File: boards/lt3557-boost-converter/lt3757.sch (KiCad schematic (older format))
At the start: 21 parts

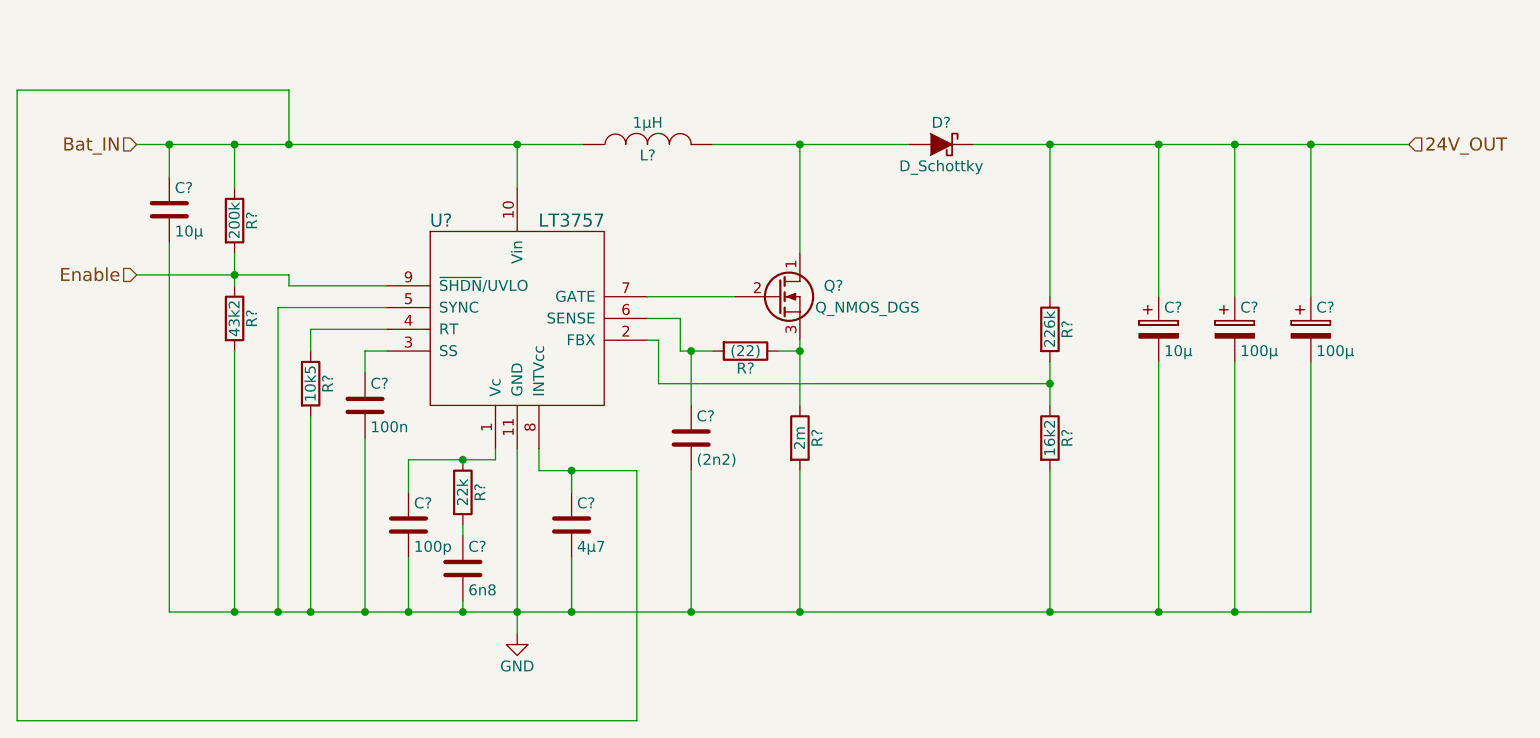
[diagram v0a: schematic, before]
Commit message: lt3557-boost-converter: schematic finished; parts selected; footprints assigned
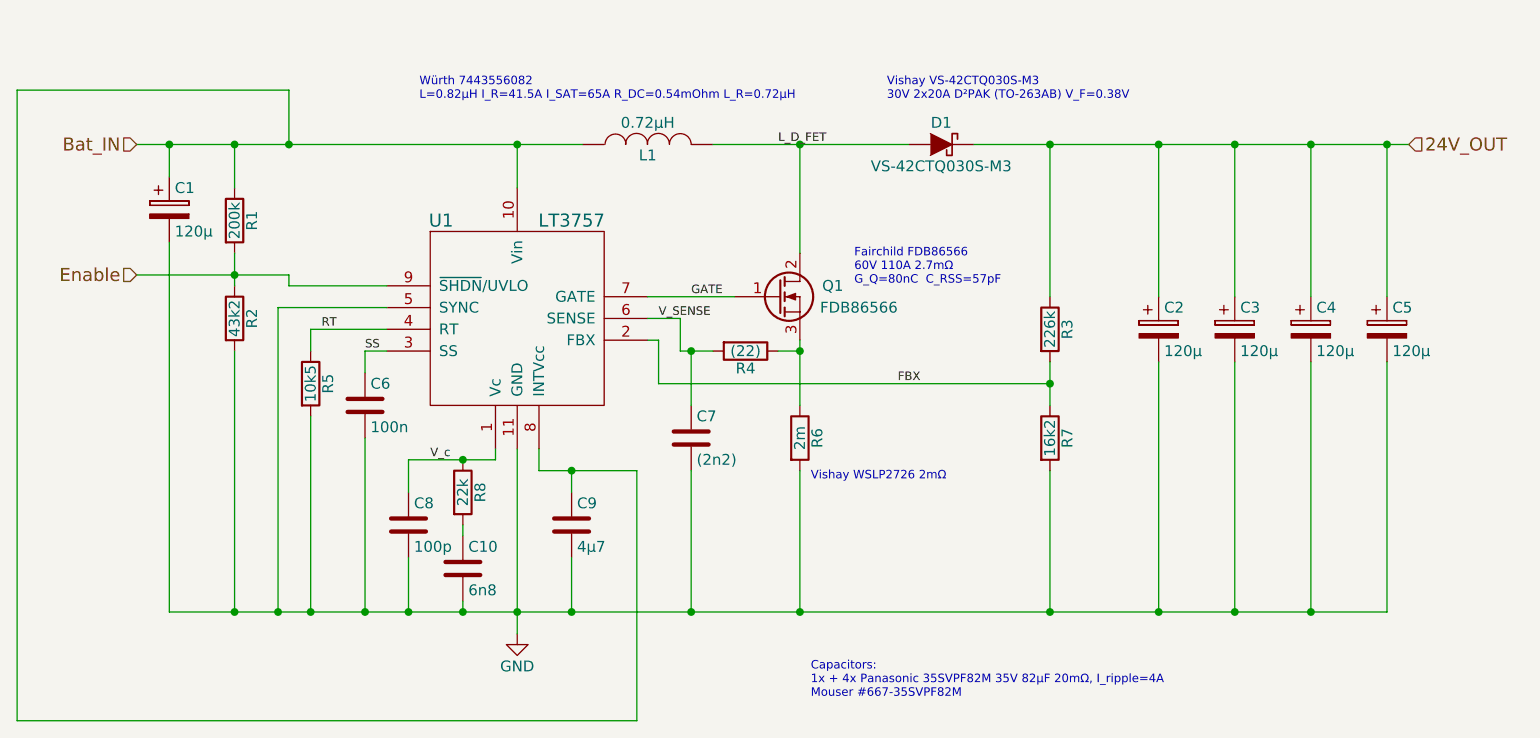
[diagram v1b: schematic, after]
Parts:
- removed C?: 10µ, symbol C
- removed Q?: Q_NMOS_DGS, symbol Q_NMOS_DGS
- added C1: 120µ, Capacitors_SMD:c_elec_8x10.5, symbol CP
- added C5: 120µ, Capacitors_SMD:c_elec_10x10.5, symbol CP
- added Q1: FDB86566, Diodes_SMD:DD-PAK_TO263_DualDiode_ThermalVias, symbol Q_NMOS_GDS
- C10, C6, C7, C8: renamed from C?; footprint (none) -> Capacitors_SMD:C_0603
- C2: renamed from C?; value 10µ -> 120µ; footprint (none) -> Capacitors_SMD:c_elec_8x10.5
- C3, C4: renamed from C?; value 100µ -> 120µ; footprint (none) -> Capacitors_SMD:c_elec_8x10.5
- C9: renamed from C?; footprint (none) -> Capacitors_SMD:C_0805
- D1: renamed from D?; value D_Schottky -> VS-42CTQ030S-M3; footprint (none) -> Diodes_SMD:DD-PAK_TO263_DualDiode_ThermalVias
- L1: renamed from L?; value 1µH -> 0.72µH; footprint (none) -> GH_Inductors:Inductor_Wurth_HCI-1890
- R1, R2, R3, R4, R5, R7, R8: renamed from R?; footprint (none) -> Resistors_SMD:R_0603
- R6: renamed from R?; footprint (none) -> resistor-power-shunt:WSLP2726
- U1: renamed from U?; footprint (none) -> Housings_SSOP:MSOP-10-1EP_3x3mm_Pitch0.5mm
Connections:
- net 24V_OUT: now also C5.1
- net Bat_IN: now also C1.1
- net GND: now also C1.2, C5.2
- net V_c: now reaches C8.1, R8.1, U1.1 (Vc)
- net FBX: now reaches R3.2, R7.1, U1.2 (FBX)
- net SS: now reaches C6.1, U1.3 (SS)
- net RT: now reaches R5.1, U1.4 (RT)
- net V_SENSE: now reaches C7.1, R4.2, U1.6 (SENSE)
- net GATE: now reaches U1.7 (GATE)
- net GATE: now also Q1.1 (G)
- net L_D_FET: now reaches D1.2 (A), L1.2
- net L_D_FET: now also Q1.2 (D)
- net at R4.1, R6.1: now also Q1.3 (S)
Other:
- note added: "Capacitors:\n1x + 4x Panasonic 35SVPF82M 35V 82µF 20mΩ, I_ripple=4A\nMouser #667-35SVPF82M"
- note added: "Fairchild FDB86566\n60V 110A 2.7mΩ\nG_Q=80nC C_RSS=57pF"
- note added: "Vishay VS-42CTQ030S-M3\n30V 2x20A D²PAK (TO-263AB) V_F=0.38V"
- note added: "Vishay WSLP2726 2mΩ"
- note added: "Würth 7443556082\nL=0.82µH I_R=41.5A I_SAT=65A R_DC=0.54mOhm L_R=0.72µH"
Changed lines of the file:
@@
 24V_OUT
 $Comp
-L GND #PWR?
+L GND #PWR03
 U 1 1 588F90A8
 P 4600 3550
-F 0 "#PWR?" H 4600 3300 50  0001 C CNN
+F 0 "#PWR03" H 4600 3300 50  0001 C CNN
 F 1 "GND" H 4600 3400 50  0000 C CNN
 F 2 "" H 4600 3550 50  0000 C CNN
@@
 Enable
 $Comp
-L LT3757 U?
+L LT3757 U1
 U 1 1 588F9C46
 P 4600 2100
-F 0 "U?" H 4250 2550 60  0000 C CNN
+F 0 "U1" H 4250 2550 60  0000 C CNN
 F 1 "LT3757" H 4850 2550 60  0000 C CNN
-F 2 "" H 4600 2100 60  0001 C CNN
+F 2 "Housings_SSOP:MSOP-10-1EP_3x3mm_Pitch0.5mm" H 4600 2100 60  0001 C CNN
 F 3 "" H 4600 2100 60  0001 C CNN
 	1    4600 2100
@@
 	4600 1300 4600 1500
 $Comp
-L INDUCTOR L?
+L INDUCTOR L1
 U 1 1 588F9D48
 P 5200 1300
-F 0 "L?" V 5150 1300 50  0000 C CNN
-F 1 "1µH" V 5300 1300 50  0000 C CNN
-F 2 "" H 5200 1300 50  0000 C CNN
+F 0 "L1" V 5150 1300 50  0000 C CNN
+F 1 "0.72µH" V 5300 1300 50  0000 C CNN
+F 2 "GH_Inductors:Inductor_Wurth_HCI-1890" H 5200 1300 50  0001 C CNN
 F 3 "" H 5200 1300 50  0000 C CNN
 	1    5200 1300
@@
 $EndComp
 $Comp
-L D_Schottky D?
+L D_Schottky D1
 U 1 1 588F9DE1
 P 6550 1300
-F 0 "D?" H 6550 1400 50  0000 C CNN
-F 1 "D_Schottky" H 6550 1200 50  0000 C CNN
-F 2 "" H 6550 1300 50  0000 C CNN
+F 0 "D1" H 6550 1400 50  0000 C CNN
+F 1 "VS-42CTQ030S-M3" H 6550 1200 50  0000 C CNN
+F 2 "Diodes_SMD:DD-PAK_TO263_DualDiode_ThermalVias" H 6550 1300 50  0001 C CNN
 F 3 "" H 6550 1300 50  0000 C CNN
 	1    6550 1300
@@
 $EndComp
 $Comp
-L Q_NMOS_DGS Q?
-U 1 1 588F9EA6
-P 5800 2000
-F 0 "Q?" H 6100 2050 50  0000 R CNN
-F 1 "Q_NMOS_DGS" H 6450 1950 50  0000 R CNN
-F 2 "" H 6000 2100 50  0000 C CNN
-F 3 "" H 5800 2000 50  0000 C CNN
-	1    5800 2000
-	1    0    0    -1
-$EndComp
-$Comp
-L R R?
+L R R6
 U 1 1 588F9F5B
 P 5900 2650
-F 0 "R?" V 5980 2650 50  0000 C CNN
+F 0 "R6" V 5980 2650 50  0000 C CNN
 F 1 "2m" V 5900 2650 50  0000 C CNN
-F 2 "" V 5830 2650 50  0000 C CNN
+F 2 "resistor-power-shunt:WSLP2726" V 5830 2650 50  0001 C CNN
 F 3 "" H 5900 2650 50  0000 C CNN
 	1    5900 2650
@@
 $EndComp
 $Comp
-L R R?
+L R R3
 U 1 1 588FA0E6
 P 7050 2150
-F 0 "R?" V 7130 2150 50  0000 C CNN
+F 0 "R3" V 7130 2150 50  0000 C CNN
 F 1 "226k" V 7050 2150 50  0000 C CNN
-F 2 "" V 6980 2150 50  0000 C CNN
+F 2 "Resistors_SMD:R_0603" V 6980 2150 50  0001 C CNN
 F 3 "" H 7050 2150 50  0000 C CNN
 	1    7050 2150
@@
 $EndComp
 $Comp
-L R R?
+L R R7
 U 1 1 588FA11B
 P 7050 2650
-F 0 "R?" V 7130 2650 50  0000 C CNN
+F 0 "R7" V 7130 2650 50  0000 C CNN
 F 1 "16k2" V 7050 2650 50  0000 C CNN
-F 2 "" V 6980 2650 50  0000 C CNN
+F 2 "Resistors_SMD:R_0603" V 6980 2650 50  0001 C CNN
 F 3 "" H 7050 2650 50  0000 C CNN
 	1    7050 2650
@@
 $EndComp
 $Comp
-L CP C?
+L CP C2
 U 1 1 588FA17F
 P 7550 2150
-F 0 "C?" H 7575 2250 50  0000 L CNN
-F 1 "10µ" H 7575 2050 50  0000 L CNN
-F 2 "" H 7588 2000 50  0000 C CNN
+F 0 "C2" H 7575 2250 50  0000 L CNN
+F 1 "120µ" H 7575 2050 50  0000 L CNN
+F 2 "Capacitors_SMD:c_elec_8x10.5" H 7588 2000 50  0001 C CNN
 F 3 "" H 7550 2150 50  0000 C CNN
 	1    7550 2150
@@
 $EndComp
 $Comp
-L CP C?
+L CP C3
 U 1 1 588FA2C0
 P 7900 2150
-F 0 "C?" H 7925 2250 50  0000 L CNN
-F 1 "100µ" H 7925 2050 50  0000 L CNN
-F 2 "" H 7938 2000 50  0000 C CNN
+F 0 "C3" H 7925 2250 50  0000 L CNN
+F 1 "120µ" H 7925 2050 50  0000 L CNN
+F 2 "Capacitors_SMD:c_elec_8x10.5" H 7938 2000 50  0001 C CNN
 F 3 "" H 7900 2150 50  0000 C CNN
 	1    7900 2150
@@
 $EndComp
 $Comp
-L CP C?
+L CP C4
 U 1 1 588FA2F5
 P 8250 2150
-F 0 "C?" H 8275 2250 50  0000 L CNN
-F 1 "100µ" H 8275 2050 50  0000 L CNN
-F 2 "" H 8288 2000 50  0000 C CNN
+F 0 "C4" H 8275 2250 50  0000 L CNN
+F 1 "120µ" H 8275 2050 50  0000 L CNN
+F 2 "Capacitors_SMD:c_elec_8x10.5" H 8288 2000 50  0001 C CNN
 F 3 "" H 8250 2150 50  0000 C CNN
 	1    8250 2150
@@
 $EndComp
 $Comp
-L R R?
+L R R2
 U 1 1 588FA451
 P 3300 2100
-F 0 "R?" V 3380 2100 50  0000 C CNN
+F 0 "R2" V 3380 2100 50  0000 C CNN
 F 1 "43k2" V 3300 2100 50  0000 C CNN
-F 2 "" V 3230 2100 50  0000 C CNN
+F 2 "Resistors_SMD:R_0603" V 3230 2100 50  0001 C CNN
 F 3 "" H 3300 2100 50  0000 C CNN
 	1    3300 2100
@@
 $EndComp
 $Comp
-L R R?
+L R R1
 U 1 1 588FA49A
 P 3300 1650
-F 0 "R?" V 3380 1650 50  0000 C CNN
+F 0 "R1" V 3380 1650 50  0000 C CNN
 F 1 "200k" V 3300 1650 50  0000 C CNN
-F 2 "" V 3230 1650 50  0000 C CNN
+F 2 "Resistors_SMD:R_0603" V 3230 1650 50  0001 C CNN
 F 3 "" H 3300 1650 50  0000 C CNN
 	1    3300 1650
 	1    0    0    -1
 $EndComp
-$Comp
-L C C?
-U 1 1 588FA4D4
-P 3000 1600
-F 0 "C?" H 3025 1700 50  0000 L CNN
-F 1 "10µ" H 3025 1500 50  0000 L CNN
-F 2 "" H 3038 1450 50  0000 C CNN
-F 3 "" H 3000 1600 50  0000 C CNN
-	1    3000 1600
-	1    0    0    -1
-$EndComp
 Wire Wire Line
 	3000 1450 3000 1300
@@
 	3000 1750 3000 3450
 $Comp
-L R R?
+L R R5
 U 1 1 588FA63C
 P 3650 2400
-F 0 "R?" V 3730 2400 50  0000 C CNN
+F 0 "R5" V 3730 2400 50  0000 C CNN
 F 1 "10k5" V 3650 2400 50  0000 C CNN
-F 2 "" V 3580 2400 50  0000 C CNN
+F 2 "Resistors_SMD:R_0603" V 3580 2400 50  0001 C CNN
 F 3 "" H 3650 2400 50  0000 C CNN
 	1    3650 2400
@@
 $EndComp
 $Comp
-L C C?
+L C C6
 U 1 1 588FA6E1
 P 3900 2500
-F 0 "C?" H 3925 2600 50  0000 L CNN
+F 0 "C6" H 3925 2600 50  0000 L CNN
 F 1 "100n" H 3925 2400 50  0000 L CNN
-F 2 "" H 3938 2350 50  0000 C CNN
+F 2 "Capacitors_SMD:C_0603" H 3938 2350 50  0001 C CNN
 F 3 "" H 3900 2500 50  0000 C CNN
 	1    3900 2500
@@
 	3500 2050 3500 3450
 Wire Wire Line
-	3000 3450 8250 3450
+	3000 3450 8600 3450
 Wire Wire Line
 	4600 2700 4600 3550
@@
 Connection ~ 8250 1300
 $Comp
-L R R?
+L R R8
 U 1 1 588FB43F
 P 4350 2900
-F 0 "R?" V 4430 2900 50  0000 C CNN
+F 0 "R8" V 4430 2900 50  0000 C CNN
 F 1 "22k" V 4350 2900 50  0000 C CNN
-F 2 "" V 4280 2900 50  0000 C CNN
+F 2 "Resistors_SMD:R_0603" V 4280 2900 50  0001 C CNN
 F 3 "" H 4350 2900 50  0000 C CNN
 	1    4350 2900
@@
 $EndComp
 $Comp
-L C C?
+L C C10
 U 1 1 588FB4B3
 P 4350 3250
-F 0 "C?" H 4375 3350 50  0000 L CNN
+F 0 "C10" H 4375 3350 50  0000 L CNN
 F 1 "6n8" H 4375 3150 50  0000 L CNN
-F 2 "" H 4388 3100 50  0000 C CNN
+F 2 "Capacitors_SMD:C_0603" H 4388 3100 50  0001 C CNN
 F 3 "" H 4350 3250 50  0000 C CNN
 	1    4350 3250
@@
 	4500 2750 4500 2700
 $Comp
-L C C?
+L C C9
 U 1 1 588FB818
 P 4850 3050
-F 0 "C?" H 4875 3150 50  0000 L CNN
+F 0 "C9" H 4875 3150 50  0000 L CNN
 F 1 "4µ7" H 4875 2950 50  0000 L CNN
-F 2 "" H 4888 2900 50  0000 C CNN
+F 2 "Capacitors_SMD:C_0805" H 4888 2900 50  0001 C CNN
 F 3 "" H 4850 3050 50  0000 C CNN
 	1    4850 3050
@@
 Connection ~ 4850 2800
 $Comp
-L C C?
+L C C8
 U 1 1 588FE63C
 P 4100 3050
-F 0 "C?" H 4125 3150 50  0000 L CNN
+F 0 "C8" H 4125 3150 50  0000 L CNN
 F 1 "100p" H 4125 2950 50  0000 L CNN
-F 2 "" H 4138 2900 50  0000 C CNN
+F 2 "Capacitors_SMD:C_0603" H 4138 2900 50  0001 C CNN
 F 3 "" H 4100 3050 50  0000 C CNN
 	1    4100 3050
@@
 	5250 2200 5250 2400
 $Comp
-L R R?
+L R R4
 U 1 1 588FE946
 P 5650 2250
-F 0 "R?" V 5730 2250 50  0000 C CNN
+F 0 "R4" V 5730 2250 50  0000 C CNN
 F 1 "(22)" V 5650 2250 50  0000 C CNN
-F 2 "" V 5580 2250 50  0000 C CNN
+F 2 "Resistors_SMD:R_0603" V 5580 2250 50  0001 C CNN
 F 3 "" H 5650 2250 50  0000 C CNN
 	1    5650 2250
@@
 $EndComp
 $Comp
-L C C?
+L C C7
 U 1 1 588FE99D
 P 5400 2650
-F 0 "C?" H 5425 2750 50  0000 L CNN
+F 0 "C7" H 5425 2750 50  0000 L CNN
 F 1 "(2n2)" H 5425 2550 50  0000 L CNN
-F 2 "" H 5438 2500 50  0000 C CNN
+F 2 "Capacitors_SMD:C_0603" H 5438 2500 50  0001 C CNN
 F 3 "" H 5400 2650 50  0000 C CNN
 	1    5400 2650
@@
 	5400 2800 5400 3450
 Connection ~ 5400 3450
+Text Notes 4150 1100 0    39   ~ 0
+Würth 7443556082\nL=0.82µH I_R=41.5A I_SAT=65A R_DC=0.54mOhm L_R=0.72µH
+Text Notes 6300 1100 0    39   ~ 0
+Vishay VS-42CTQ030S-M3\n30V 2x20A D²PAK (TO-263AB) V_F=0.38V
+$Comp
+L CP C1
+U 1 1 58924C20
+P 3000 1600
+F 0 "C1" H 3025 1700 50  0000 L CNN
+F 1 "120µ" H 3025 1500 50  0000 L CNN
+F 2 "Capacitors_SMD:c_elec_8x10.5" H 3038 1450 50  0001 C CNN
+F 3 "" H 3000 1600 50  0000 C CNN
+	1    3000 1600
+	1    0    0    -1
+$EndComp
+Text Notes 5950 3850 0    39   ~ 0
+Capacitors:\n1x + 4x Panasonic 35SVPF82M 35V 82µF 20mΩ, I_ripple=4A\nMouser #667-35SVPF82M
+$Comp
+L CP C5
+U 1 1 58924E09
+P 8600 2150
+F 0 "C5" H 8625 2250 50  0000 L CNN
+F 1 "120µ" H 8625 2050 50  0000 L CNN
+F 2 "Capacitors_SMD:c_elec_10x10.5" H 8638 2000 50  0001 C CNN
+F 3 "" H 8600 2150 50  0000 C CNN
+	1    8600 2150
+	1    0    0    -1
+$EndComp
+Wire Wire Line
+	8600 2000 8600 1300
+Connection ~ 8600 1300
+Wire Wire Line
+	8600 3450 8600 2300
+Connection ~ 8250 3450
+Text Notes 5950 2850 0    39   ~ 0
+Vishay WSLP2726 2mΩ
+$Comp
+L Q_NMOS_GDS Q1
+U 1 1 58928FBF
+P 5800 2000
+F 0 "Q1" H 6100 2050 50  0000 R CNN
+F 1 "FDB86566" H 6350 1950 50  0000 R CNN
+F 2 "Diodes_SMD:DD-PAK_TO263_DualDiode_ThermalVias" H 6000 2100 50  0001 C CNN
+F 3 "" H 5800 2000 50  0000 C CNN
+	1    5800 2000
+	1    0    0    -1
+$EndComp
+Text Notes 6150 1950 0    39   ~ 0
+Fairchild FDB86566\n60V 110A 2.7mΩ\nG_Q=80nC  C_RSS=57pF
+Text Label 5250 2100 0    39   ~ 0
+V_SENSE
+Text Label 6350 2400 0    39   ~ 0
+FBX
+Text Label 5400 2000 0    39   ~ 0
+GATE
+Text Label 4200 2750 0    39   ~ 0
+V_c
+Text Label 3700 2150 0    39   ~ 0
+RT
+Text Label 3900 2250 0    39   ~ 0
+SS
+Text Label 5800 1300 0    39   ~ 0
+L_D_FET
 $EndSCHEMATC

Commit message: lt3557-boost-converter: layout
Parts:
- C5: footprint Capacitors_SMD:c_elec_10x10.5 -> Capacitors_SMD:c_elec_8x10.5
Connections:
- net GND: now also R6.1; no longer R6.2
- net at Q1.3 (S), R4.1: now also R6.2; no longer R6.1
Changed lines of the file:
@@
 F 3 "" H 5900 2650 50  0000 C CNN
 	1    5900 2650
-	1    0    0    -1
+	-1   0    0    1
 $EndComp
 $Comp
@@
 F 0 "C5" H 8625 2250 50  0000 L CNN
 F 1 "120µ" H 8625 2050 50  0000 L CNN
-F 2 "Capacitors_SMD:c_elec_10x10.5" H 8638 2000 50  0001 C CNN
+F 2 "Capacitors_SMD:c_elec_8x10.5" H 8638 2000 50  0001 C CNN
 F 3 "" H 8600 2150 50  0000 C CNN
 	1    8600 2150

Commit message: lt3757-board: fix diode polarity in schematic and layout
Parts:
- removed D1: VS-42CTQ030S-M3, Diodes_SMD:DD-PAK_TO263_DualDiode_ThermalVias, symbol D_Schottky
- added D1: VS-42CTQ030S-M3, Diodes_SMD:DD-PAK_TO263_DualDiode_ThermalVias, symbol D_Schottky_x2_KCom_AKA
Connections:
- net 24V_OUT: now also D1.2 (K)
- net L_D_FET: now also D1.1 (A), D1.3 (A)
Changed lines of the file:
@@
-$EndComp
-$Comp
-L D_Schottky D1
-U 1 1 588F9DE1
-P 6550 1300
-F 0 "D1" H 6550 1400 50  0000 C CNN
-F 1 "VS-42CTQ030S-M3" H 6550 1200 50  0000 C CNN
-F 2 "Diodes_SMD:DD-PAK_TO263_DualDiode_ThermalVias" H 6550 1300 50  0001 C CNN
-F 3 "" H 6550 1300 50  0000 C CNN
-	1    6550 1300
-	-1   0    0    -1
 $EndComp
 $Comp
@@
 Connection ~ 4600 1300
 Wire Wire Line
-	5500 1300 6400 1300
-Wire Wire Line
-	5900 1800 5900 1300
+	5900 1300 5900 1800
 Connection ~ 5900 1300
 Wire Wire Line
@@
 Wire Wire Line
 	7050 2000 7050 1300
-Wire Wire Line
-	6700 1300 8700 1300
 Wire Wire Line
 	8250 1300 8250 2000
@@
 Text Notes 4150 1100 0    39   ~ 0
 Würth 7443556082\nL=0.82µH I_R=41.5A I_SAT=65A R_DC=0.54mOhm L_R=0.72µH
-Text Notes 6300 1100 0    39   ~ 0
+Text Notes 5950 850  0    39   ~ 0
 Vishay VS-42CTQ030S-M3\n30V 2x20A D²PAK (TO-263AB) V_F=0.38V
 $Comp
@@
 Text Label 5800 1300 0    39   ~ 0
 L_D_FET
+$Comp
+L D_Schottky_x2_KCom_AKA D1
+U 1 1 58A9C328
+P 6450 1300
+F 0 "D1" V 6350 1150 50  0000 C CNN
+F 1 "VS-42CTQ030S-M3" V 6100 1300 50  0000 C CNN
+F 2 "Diodes_SMD:DD-PAK_TO263_DualDiode_ThermalVias" H 6450 1300 50  0001 C CNN
+F 3 "" H 6450 1300 50  0000 C CNN
+	1    6450 1300
+	0    -1   -1   0
+$EndComp
+Wire Wire Line
+	5500 1300 6250 1300
+Wire Wire Line
+	6250 1000 6250 1600
+Wire Wire Line
+	6250 1000 6450 1000
+Wire Wire Line
+	6250 1600 6450 1600
+Connection ~ 6250 1300
+Wire Wire Line
+	6650 1300 8700 1300
 $EndSCHEMATC
